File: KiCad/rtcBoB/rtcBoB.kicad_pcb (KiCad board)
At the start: 2 copper layers, 30.5 x 30.5 mm, 16 parts, among them P1 CDOT1, P2 CDOT2, P3 CONN_2, U1 DS3231

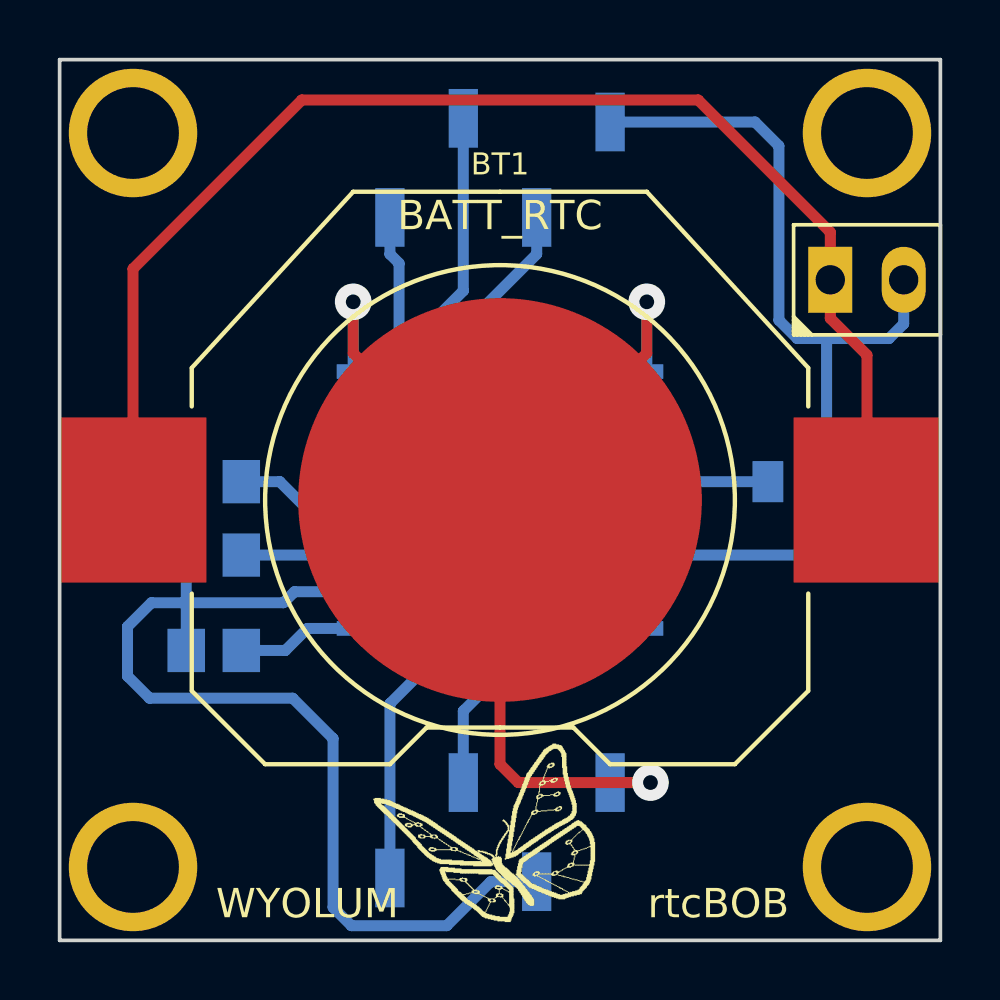
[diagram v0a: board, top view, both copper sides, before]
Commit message: rtcBoB_v2 : All SMD version. Gerbers ready for production.
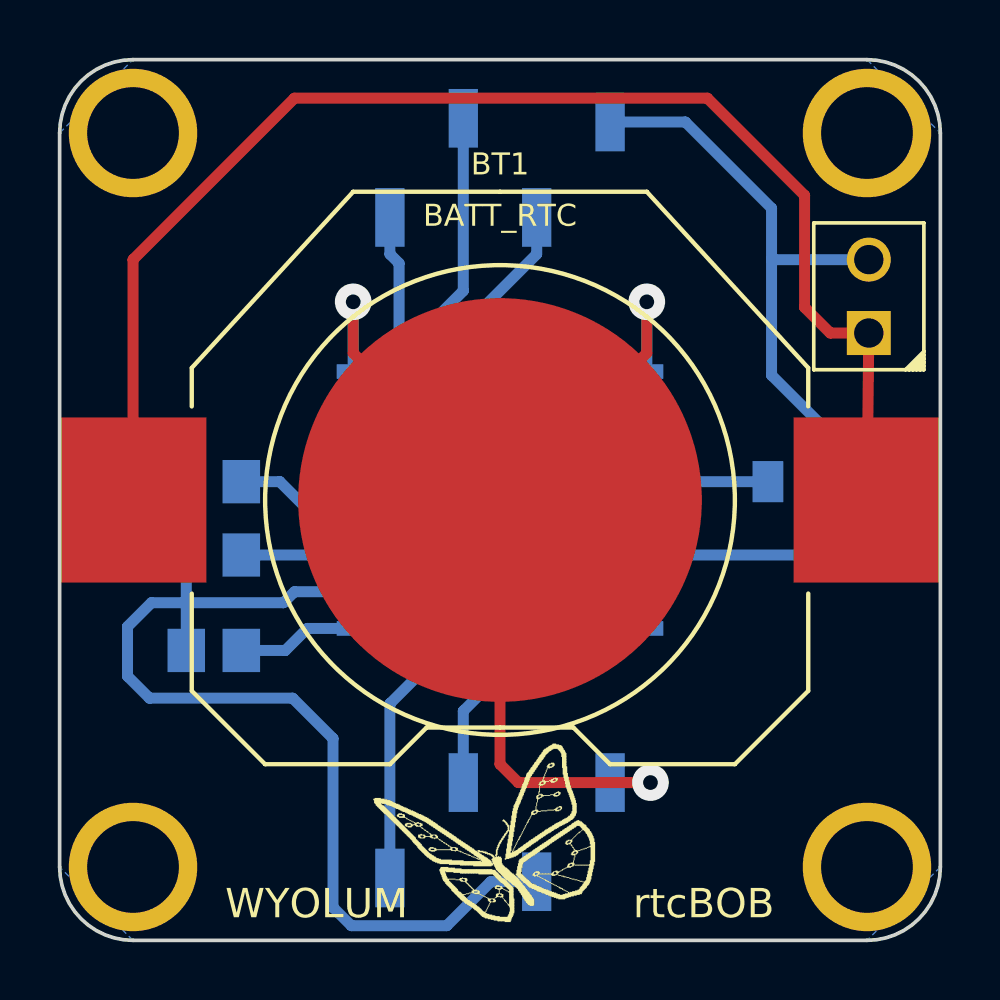
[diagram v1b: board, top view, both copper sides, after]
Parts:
- moved P3 0.58 mm to (53.4, 33.6), turned to 90 degrees
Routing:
- net /BAT: track 31.8 -> 28.7 mm
- net N-000005: track 46.2 -> 47.5 mm
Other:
- outline, holes or cut-outs redrawn
- board text added: "ver2"
